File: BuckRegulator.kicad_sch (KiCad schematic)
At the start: 28 parts, among them J8 Conn_01x03_Pin, SW1 SW_DIP_x04, U6 AMS1117, U7 LM2596HVS-ADJRG

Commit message: Schematic
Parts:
- removed R26: 9.53k, PCM_JLCPCB:R_0402, symbol Device:R
- removed R27: 5.11k, PCM_JLCPCB:R_0402, symbol Device:R
- removed SW1: SW_DIP_x04, Button_Switch_THT:SW_DIP_SPSTx04_Slide_6.7x11.72mm_W7.62mm_P2.54mm_LowProfile, symbol Switch:SW_DIP_x04
- renumbered C20 to C10, C21 to C11, C22 to C12, C23 to C13, C24 to C14, C50 to C15, C17 to C7, C19 to C8, C51 to C9, D6 to D5, D5 to D6, D10 to D7, D4 to D8, J8 to J7, R21 to R44, R22 to R45, R23 to R46, R25 to R47, R24 to R48, R28 to R49, R29 to R50, TP8 to TP1, U6 to U5, U7 to U6
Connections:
- net at C12.1, R46.2, R48.1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: now also R47.1
- no-connect marks 2 -> 0
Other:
- note removed: "6.2V"
- note removed: "9V"
- note removed: "Buck converter Volage selector 1-8 -> 24V 2-7 -> 12V 3-6 -> 9V 4-5 -> 6.2V"

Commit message: reviev by Wojtek
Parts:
- removed C7, C8: 10uF, PCM_JLCPCB:C_0603, symbol PCM_JLCPCB-Capacitors:0603,10uF
- removed D5, D6, D7: SS510C, SS510C:SMC_L7.1-W6.2-LS8.1-RD, symbol SS510C:SS510C
- removed R46: 1kΩ, PCM_JLCPCB:R_0402, symbol PCM_JLCPCB-Resistors:0402,1kΩ
- removed R47: 16.5k, PCM_JLCPCB:R_0402, symbol Device:R
- removed R48: 18.7k, PCM_JLCPCB:R_0402, symbol Device:R
- removed U5: AMS1117, PCM_JLCPCB:SOT-223-3_L6.5-W3.4-P2.30-LS7.0-BR, symbol PCM_JLCPCB-Power:LDO, 3.3V, 1A
- added R46: 3.9kΩ, PCM_JLCPCB:R_0402, symbol PCM_JLCPCB-Resistors:0402,3.9kΩ
- added R47: 33kΩ, PCM_JLCPCB:R_0402, symbol PCM_JLCPCB-Resistors:0402,33kΩ
- added R48: 1.2kΩ, PCM_JLCPCB:R_0402, symbol PCM_JLCPCB-Resistors:0402,1.2kΩ
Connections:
- net U_reg is gone; now on net 12V: C12.2, C13.1, C15.1, L1.2, R49.1, TP1.1
- net GND: now also R46.1
- net at C12.1, U6.4 (FB): now also R46.2, R47.1
- net 12V: now reaches J7.3 (Pin_3)
- net 12V: now also R48.2
- new net: R47.2, R48.1
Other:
- note added: "Uout = 1.23 * (1 + Rhigh/Rlow) = 12.016V"
- note removed: "12V"
- note removed: "24V default must be connected at all times"
- note removed: "3V3 LDO"
- note removed: "Diodes to drop voltage from chainbus max 48V to 46V for TMC5130A-TA to handle"
- note removed: "LM2596 Step-Down Regulator"
- note removed: "R2 = R1(Vout/Vref-1) R1 = 1kohm 1%"
- note removed: "Uout = 1.23*(1+r2/r1)"
- moved on the sheet: C12

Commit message: Schematic touchup
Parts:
- removed D8: SS510C, SS510C:SMC_L7.1-W6.2-LS8.1-RD, symbol SS510C:SS510C
- added D10: SS510C, SS510C:SMC_L7.1-W6.2-LS8.1-RD, symbol SS510C:SS510C
- added D6: SS510C, PCM_JLCPCB:D_SMC, symbol PCM_JLCPCB-Diodes:Schottky,SS510C
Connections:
- net GND: now also D6.2
- net sw: now also D6.1

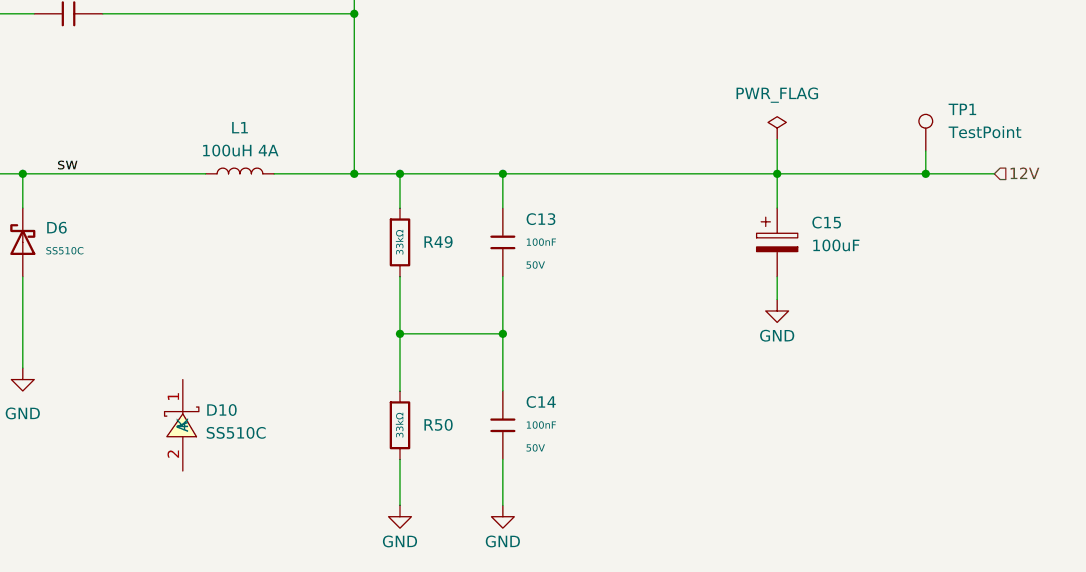
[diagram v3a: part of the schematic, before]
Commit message: PCB design
Hat allows to connect 1 LED tape at a time
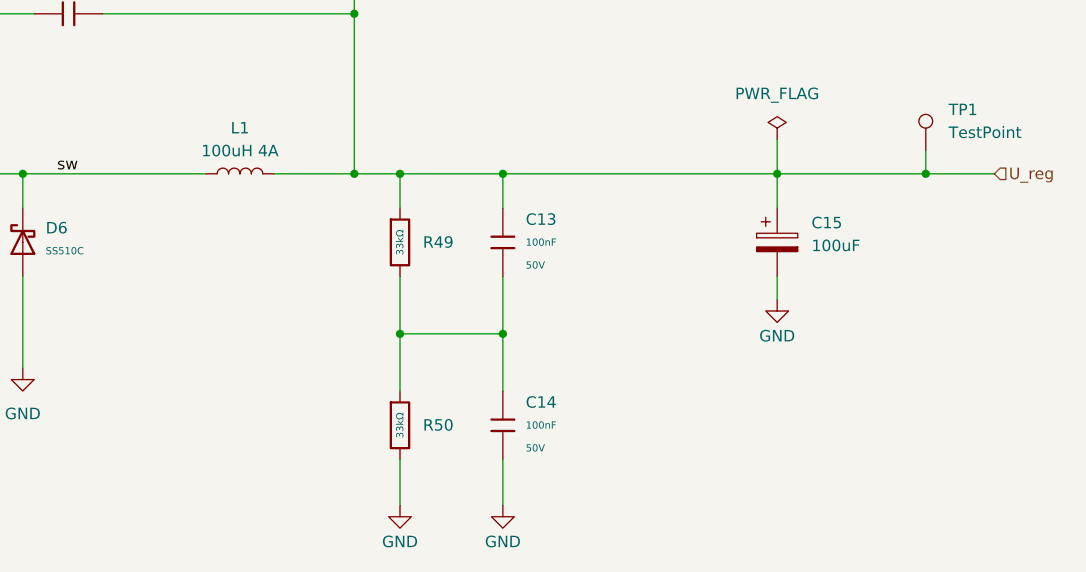
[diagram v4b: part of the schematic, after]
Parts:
- removed D10: SS510C, SS510C:SMC_L7.1-W6.2-LS8.1-RD, symbol SS510C:SS510C
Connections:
- net 12V: no longer C12.2, C13.1, C15.1, L1.2, R48.2, R49.1, TP1.1
- new net U_reg: C12.2, C13.1, C15.1, L1.2, R48.2, R49.1, TP1.1
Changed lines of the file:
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@@
 		)
 	)
-	(hierarchical_label "12V"
+	(hierarchical_label "U_reg"
 		(shape input)
 		(at 267.97 86.36 0)
@@
 					(unit 1)
 				)
-			)
-		)
-	)
-	(symbol
-		(lib_id "SS510C:SS510C")
-		(at 177.8 114.3 270)
-		(unit 1)
-		(body_style 1)
-		(exclude_from_sim no)
-		(in_bom yes)
-		(on_board yes)
-		(in_pos_files no)
-		(dnp no)
-		(fields_autoplaced yes)
-		(property "Reference" "D10"
-			(at 180.34 112.6499 90)
-			(show_name no)
-			(do_not_autoplace no)
-			(effects
-				(font
-					(size 1.27 1.27)
-				)
-				(justify left)
-			)
-		)
-		(property "Value" "SS510C"
-			(at 180.34 115.1899 90)
-			(show_name no)
-			(do_not_autoplace no)
-			(effects
-				(font
-					(size 1.27 1.27)
-				)
-				(justify left)
-			)
-		)
-		(property "Footprint" "SS510C:SMC_L7.1-W6.2-LS8.1-RD"
-			(at 170.18 114.3 0)
-			(hide yes)
-			(show_name no)
-			(do_not_autoplace no)
-			(effects
-				(font
-					(size 1.27 1.27)
-				)
-			)
-		)
-		(property "Datasheet" "https://lcsc.com/product-detail/Schottky-Barrier-Diodes-SBD_SS510C_C123944.html"
-			(at 167.64 114.3 0)
-			(hide yes)
-			(show_name no)
-			(do_not_autoplace no)
-			(effects
-				(font
-					(size 1.27 1.27)
-				)
-			)
-		)
-		(property "Description" ""
-			(at 177.8 114.3 0)
-			(hide yes)
-			(show_name no)
-			(do_not_autoplace no)
-			(effects
-				(font
-					(size 1.27 1.27)
-				)
-			)
-		)
-		(property "Manufacturer" "晶导微电子"
-			(at 165.1 114.3 0)
-			(hide yes)
-			(show_name no)
-			(do_not_autoplace no)
-			(effects
-				(font
-					(size 1.27 1.27)
-				)
-			)
-		)
-		(property "MPN" "SS510C"
-			(at 162.56 114.3 0)
-			(hide yes)
-			(show_name no)
-			(do_not_autoplace no)
-			(effects
-				(font
-					(size 1.27 1.27)
-				)
-			)
-		)
-		(property "LCSC Part" "C123944"
-			(at 160.02 114.3 0)
-			(hide yes)
-			(show_name no)
-			(do_not_autoplace no)
-			(effects
-				(font
-					(size 1.27 1.27)
-				)
-			)
-		)
-		(pin "2"
-		)
-		(pin "1"
-		)
-		(instances
-			(project "MMS3_hat_templates"
-				(path "/6596548a-44e0-46d8-8624-fd71cf4a3e17/1fa50cc0-81ad-4331-90de-681d56270af0"
-					(reference "D10")
-					(unit 1)
-				)

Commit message: PCB addjustments
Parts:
- added D10, D8: SS510C, PCM_JLCPCB:D_SMC, symbol PCM_JLCPCB-Diodes:Schottky,SS510C
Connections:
- net 12V: now also D10.1, D8.1; no longer J7.3 (Pin_3)
- net U_reg: no longer names the net of C12.2, C13.1, C15.1, L1.2, R48.2, R49.1, TP1.1
- net U_reg: now also D10.2
- new net: D8.2, J7.3 (Pin_3)
